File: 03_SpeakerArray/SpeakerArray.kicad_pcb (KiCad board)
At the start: 2 copper layers, 134.6 x 101.6 mm, 37 parts, among them J1 Screw_Terminal_01x02

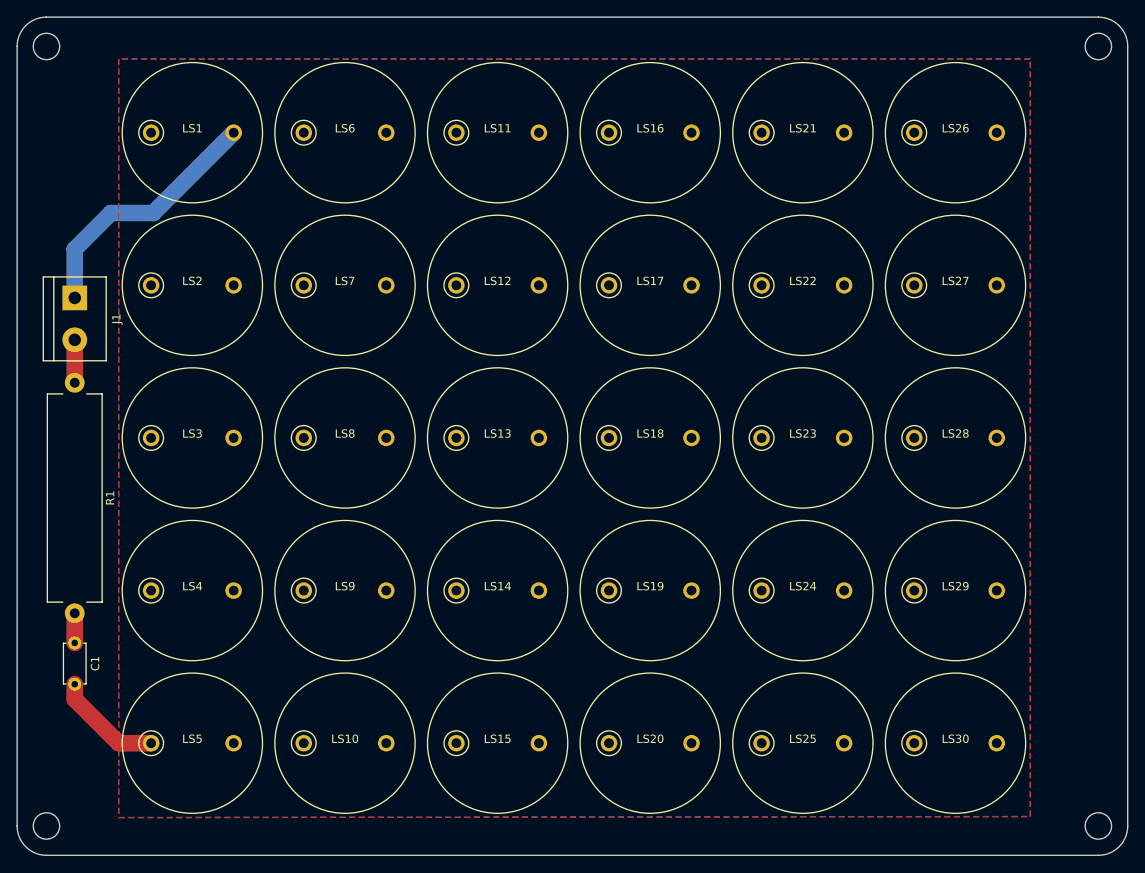
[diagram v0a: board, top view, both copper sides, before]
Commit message: 外形微調整、シルク配置
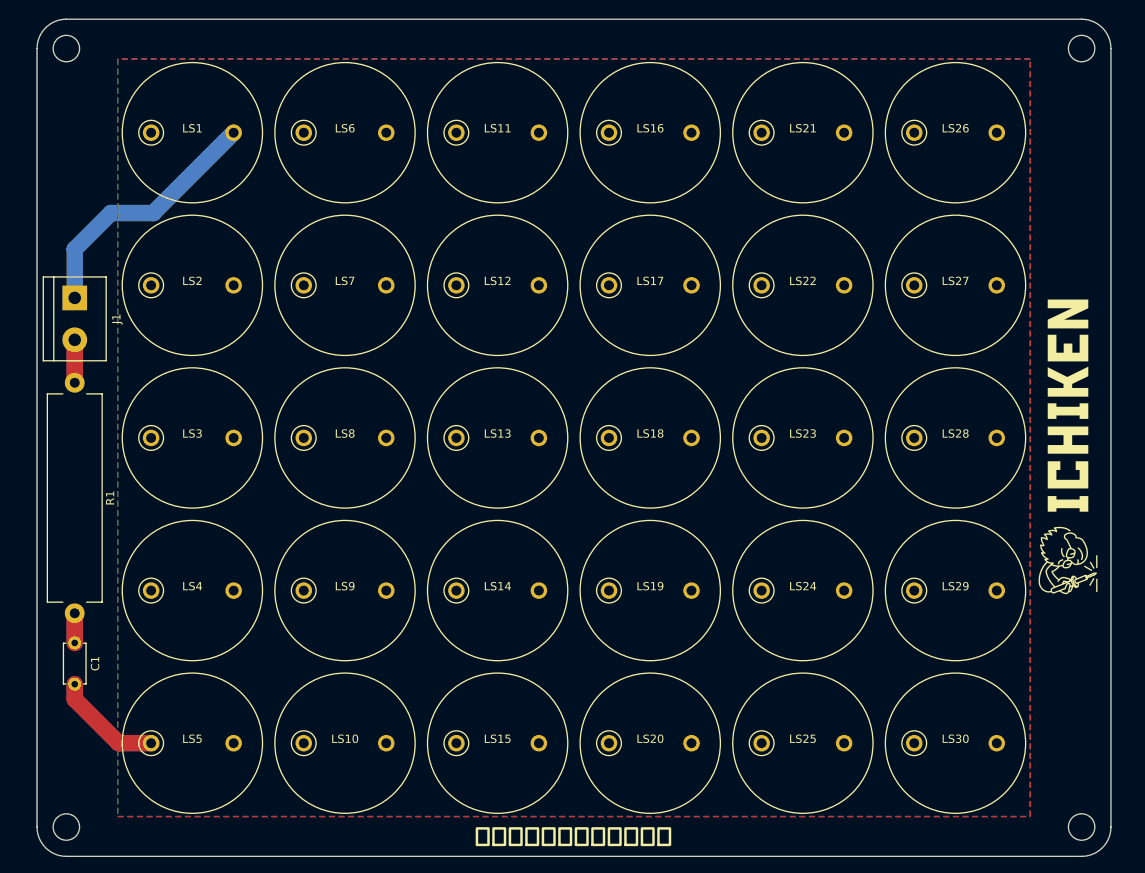
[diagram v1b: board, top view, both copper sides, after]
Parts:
- moved REF** 2.43 mm to (65.7, 29.2)
- moved REF** 2.42 mm to (65.7, 123.6)
- moved REF** 2.05 mm to (188.7, 29.2)
- moved REF** 2.04 mm to (188.7, 123.6)
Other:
- board size 134.6 x 101.6 mm -> 130.2 x 101.5 mm
- board text added: "超音波スピーカアレイ基板"

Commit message: ターミナルにシルク追加
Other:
- board text added: "GND"
- board text added: "Vo"

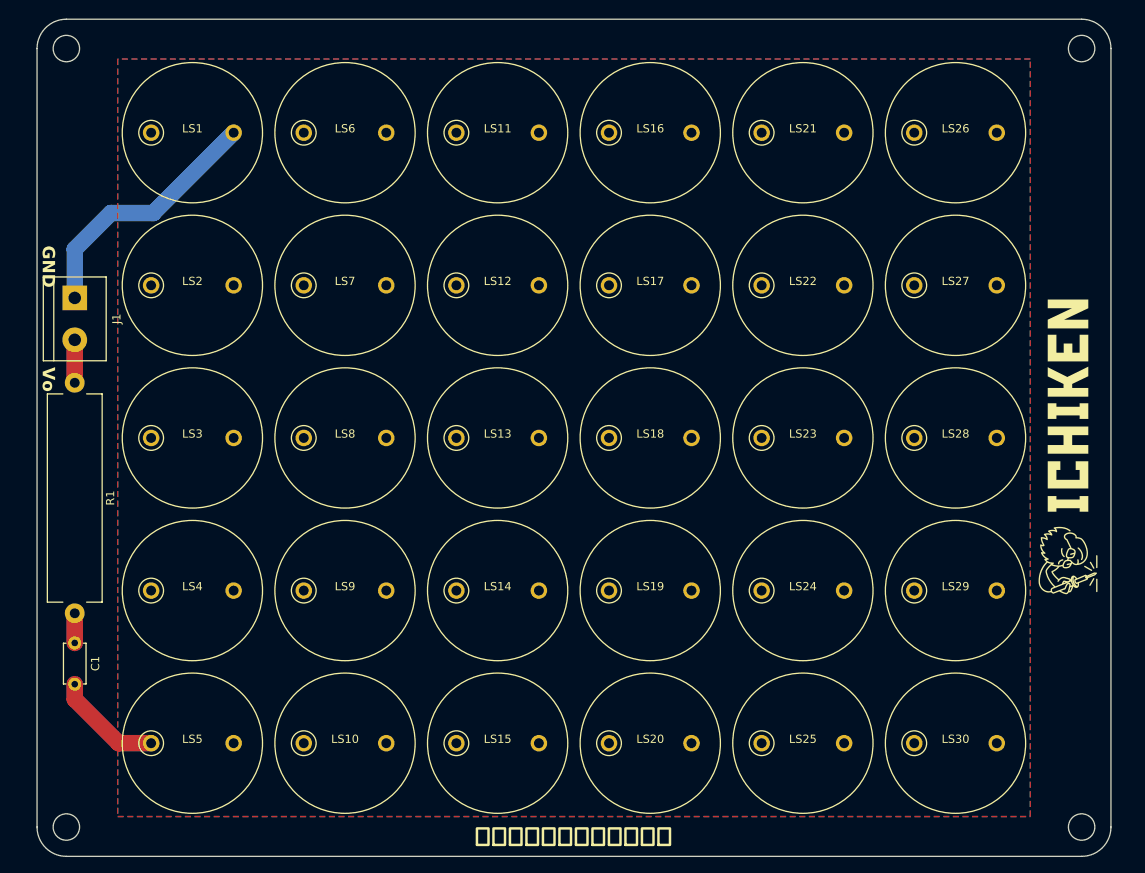
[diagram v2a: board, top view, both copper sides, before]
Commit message: ベタ除去、パターン配線のみに変更 #2
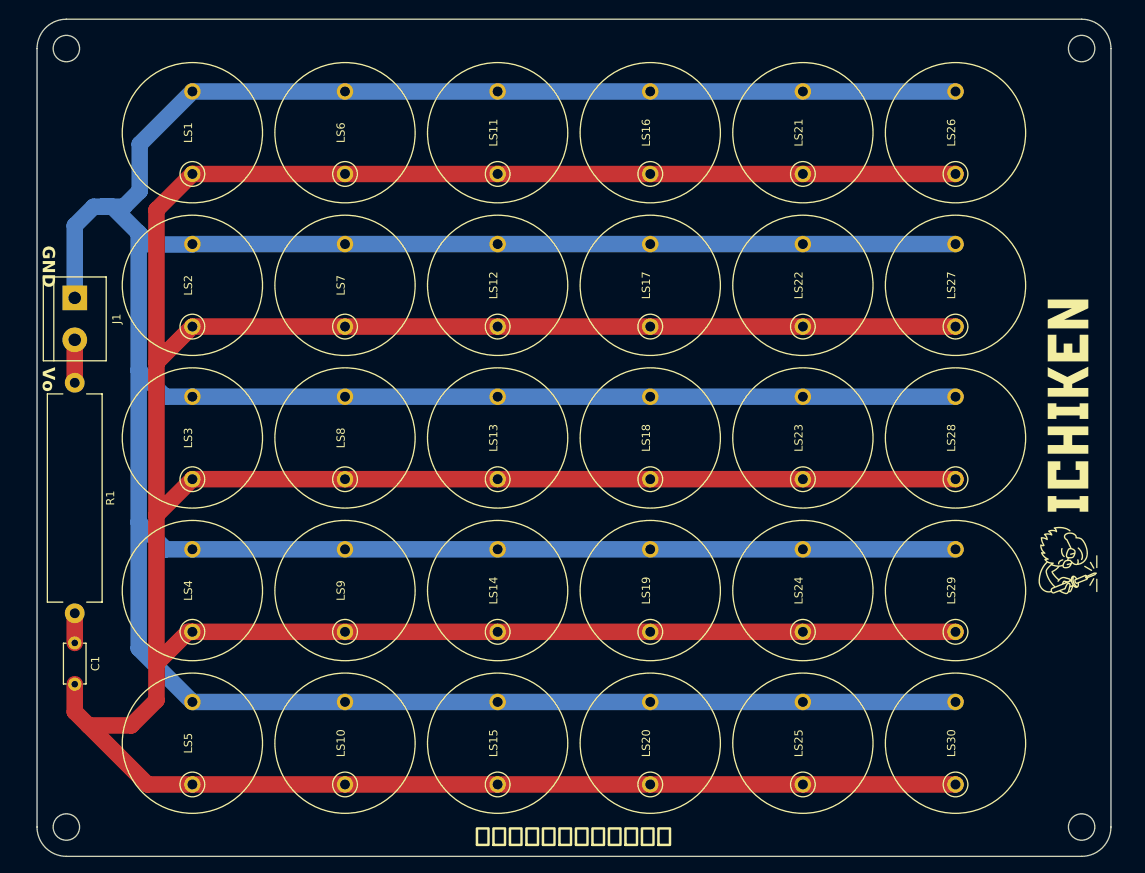
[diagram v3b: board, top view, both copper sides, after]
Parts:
- turned LS1 to 90 degrees
- turned LS10 to 90 degrees
- turned LS11 to 90 degrees
- turned LS12 to 90 degrees
- turned LS13 to 90 degrees
- turned LS14 to 90 degrees
- turned LS15 to 90 degrees
- turned LS16 to 90 degrees
- turned LS17 to 90 degrees
- turned LS18 to 90 degrees
- turned LS19 to 90 degrees
- turned LS2 to 90 degrees
- turned LS20 to 90 degrees
- turned LS21 to 90 degrees
- turned LS22 to 90 degrees
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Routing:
- net Spk+: track 13.3 -> 577.1 mm
- net Spk-: track 31.0 -> 583.7 mm
- removed copper zone on F.Cu, net Spk+
- removed copper zone on B.Cu, net Spk-
